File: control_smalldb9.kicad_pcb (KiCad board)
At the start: 2 copper layers, 140 x 110 mm, 130 parts, among them IC1 DNP, IC2 DNP, IC3 ST232BD, IC4 ATMEGA128-A, IC5 ST232BD, IC6 FT232RL, J1 DB9, J2 B, J3 USB_4, J4 POWER, J5 DB9, P1 SENSOR, P2 I2C0, P3 I2C1, P4 I2C2, P5 COIN, P6 BILL, P7 ISP, P8 CONN_2, P9 CONN_2, X1 16MHz

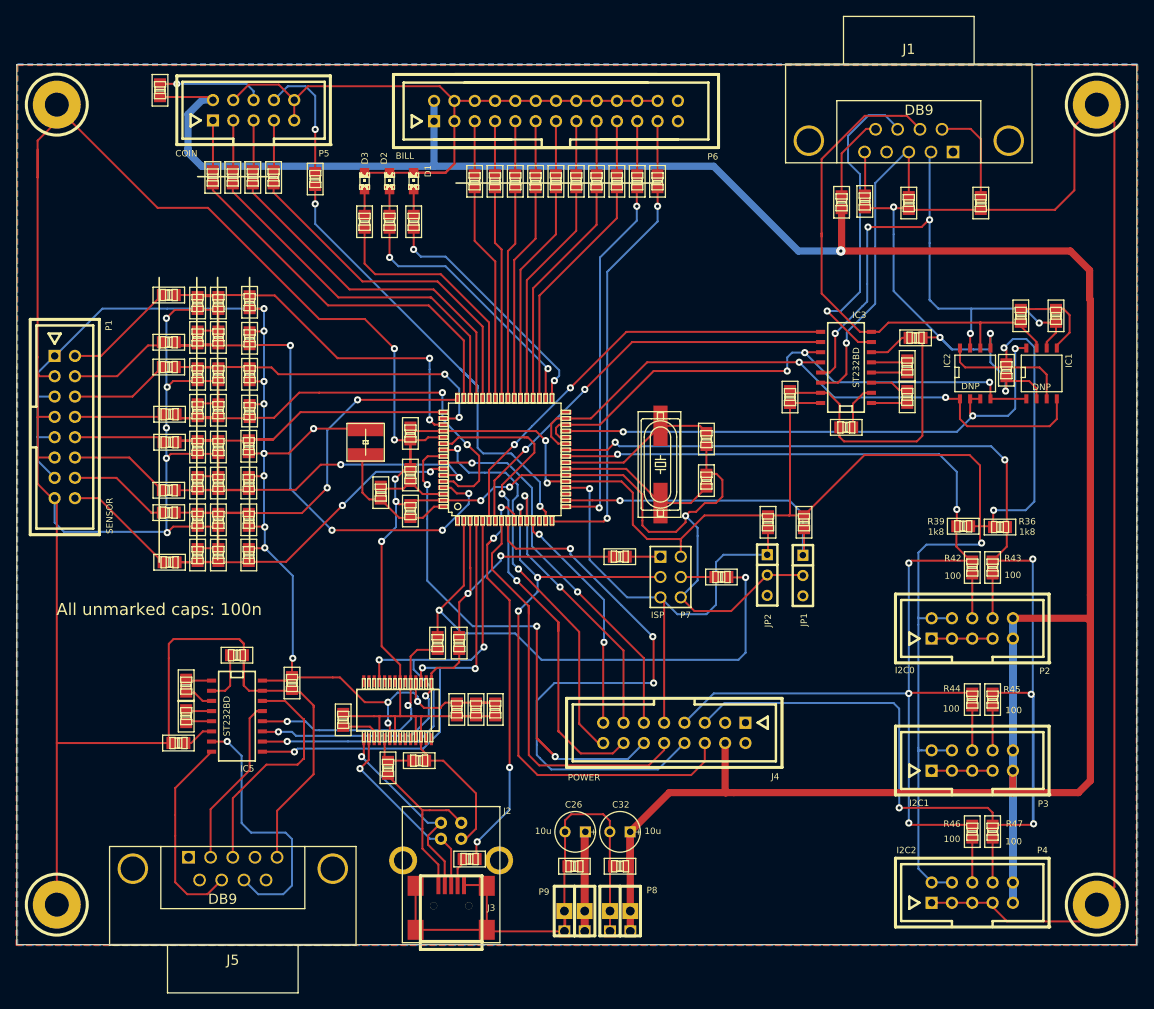
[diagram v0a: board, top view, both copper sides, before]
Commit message: Unified silk screen text sizes, fixed and relocated some text
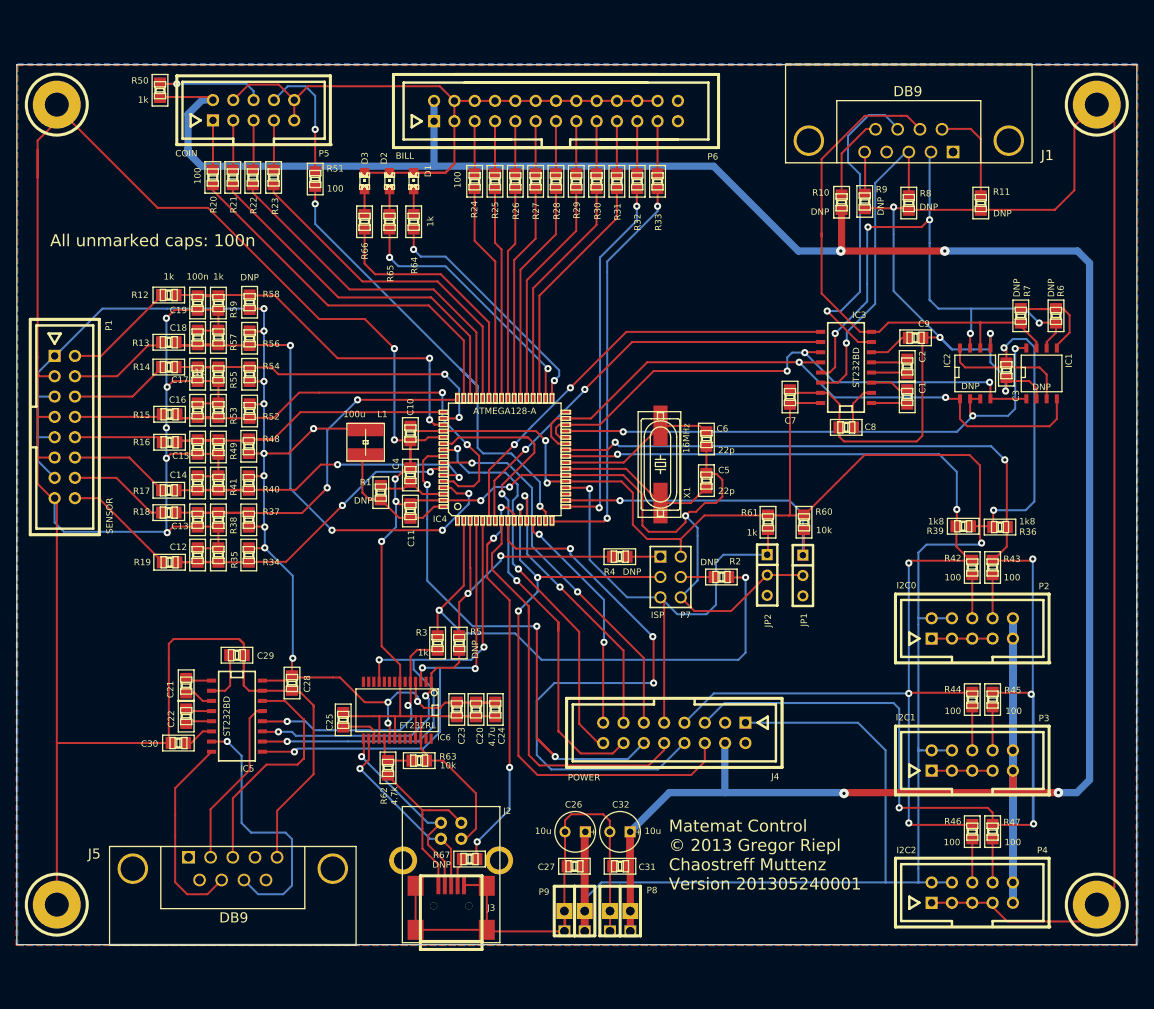
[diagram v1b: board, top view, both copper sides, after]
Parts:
- C1, C10, C11, C12, C13, C14, C15, C16, C17, C18, C19, C2, C20, C21, C22, C23, C24, C25, C27, C28, C29, C3, C30, C31, C4, C5, C6, C7, C8, C9, R1, R10, R11, R12, R13, R14, R15, R16, R17, R18, R19, R2, R20, R21, R22, R23, R24, R25, R26, R27, R28, R29, R3, R30, R31, R32, R33, R34, R35, R36, R37, R38, R39, R4, R40, R41, R42, R43, R44, R45, R46, R47, R48, R49, R5, R50, R51, R52, R53, R54, R55, R56, R57, R58, R59, R6, R60, R61, R62, R63, R64, R65, R66, R67, R7, R8, R9: footprint -R2012 -> -R0805_oni
- IC4: footprint -TQFP64 -> oni_atmel-2005-TQFP64
- IC6: footprint -SSOP28 -> SSOP28
- L1: footprint wuerth_elektronik_v5-WE-PD2_S -> oni_wuerth_elektronik_v5-WE-PD2_S
- X1: footprint crystal-SM49 -> oni_crystal-SM49
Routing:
- net VCC: track 430.0 -> 510.5 mm
- net +12V: track 412.7 -> 402.4 mm, vias 1 -> 4
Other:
- board text added: "Matemat Control © 2013 Gregor Riepl Chaostreff Muttenz Version 201305240001"
